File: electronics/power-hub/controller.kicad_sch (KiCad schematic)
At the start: 55 parts, among them J6 USB, SW1 RESET, SW2 BOOT, U2 LMR51635YDDCR, U3 AMS1117-3.3, U4 ESP32-S3-MINI-1-N8, U5 USBLC6-2SC6, U6 TCAN1044AV

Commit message: Power hub v0.5: USB-C PD input (AP33772S), 4 layers, rows off until enabled
The rack now runs from one USB PD 3.1 charger instead of the GST60A24 brick.

Hub v0.5 (76 x 140 mm, 4 layers, In1 GND, In2 VRACK/+3V3):
* AP33772S sink: 20 V at power-up (VSEL 39k), 28 V EPR on the controller's
  request, never 36/48 V; 5 mOhm Kelvin shunt, back-to-back IRF7842 switch,
  SMAJ30A TVS, NTC by the switch, interrupt and I2C to the ESP32-S3.
* USB4105 5 A receptacle; the controller's buck runs from VBUS (5-28 V),
  ahead of the switch.
* Every row's TPS26600 is off until the controller drives ROW_EN (SHDN pulled
  low); IMON per row; front PD LED.
* ERC 0, DRC 0 errors, 0 unconnected, parity 0; 146 3D models, 0 stand-ins.

Power box: 84 x 148 x 35 mm, hub only (no brick, no cradles), rear USB-C
cut-out, lid on corner lugs.  Viewer, BOM (charger + 5 A e-marked cable,
4-layer JLC estimate) and docs (power, mechanical, cabling, assembly,
electronics) follow.

Co-Authored-By: Claude Opus 5.5 <noreply@anthropic.com>
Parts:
- added TP8: PD_VCC, TestPoint:TestPoint_Pad_D1.5mm, symbol Connector:TestPoint
- C118, C119: LCSC (none) -> C53987; MPN (none) -> 0603B472K500NT; Manufacturer (none) -> FH (Guangdong Fenghua Advanced Tech)
- J6: footprint Connector_USB:USB_C_Receptacle_HRO_TYPE-C-31-M-12 -> Connector_USB:USB_C_Receptacle_GCT_USB4105-xx-A_16P_TopMnt_Horizontal; LCSC C165948 -> C5184243; MPN TYPE-C-31-M-12 -> USB4105-GF-A-120; Manufacturer Korean Hroparts -> GCT
- R205: value 1M -> 100k; LCSC C22935 -> C25803; MPN 0603WAF1004T5E -> 0603WAF1003T5E
- R206: value 100k -> 47k; LCSC C25803 -> C25819; MPN 0603WAF1003T5E -> 0603WAF4702T5E
- R211: LCSC (none) -> C23138; MPN (none) -> 0603WAF3300T5E; Manufacturer (none) -> UNI-ROYAL(Uniroyal Elec)
- R215, R216, R217, R218: value 62 -> 56; footprint Resistor_SMD:R_0805_2012Metric -> Resistor_SMD:R_0603_1608Metric; LCSC (none) -> C25196; MPN (none) -> 0603WAF560JT5E; Manufacturer (none) -> UNI-ROYAL(Uniroyal Elec)
- TP6: value +24V -> VRACK
- U3: value AMS1117-3.3 -> AP2112K-3.3TRG1; footprint Package_TO_SOT_SMD:SOT-223-3_TabPin2 -> Package_TO_SOT_SMD:SOT-23-5; symbol Regulator_Linear:AMS1117-3.3 -> Regulator_Linear:AP2112K-3.3; LCSC C6186 -> C51118; MPN AMS1117-3.3 -> AP2112K-3.3TRG1; Manufacturer AMS -> Diodes Incorporated
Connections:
- net ROW_OFF_A is gone; now on net POS_B: U4.15 (IO11)
- net ROW_OFF_B is gone; now on net POS_C: U4.16 (IO12)
- net ROW_OFF_C is gone; now on net POS_D: U4.17 (IO13)
- net +3V3: now also U3.5 (VOUT); no longer U3.2 (VO)
- net +5V: now also U3.1 (VIN)
- net CAN_RXD: now also U4.12 (IO8); no longer U4.36 (IO40)
- net CAN_STB: now also U4.13 (IO9); no longer U4.38 (IO42)
- net CAN_TXD: now also U4.11 (IO7); no longer U4.35 (IO39)
- net CTL_LED: now also U4.31 (IO35); no longer U4.37 (IO41)
- net FLT_A: now also U4.22 (IO18); no longer U4.11 (IO7)
- net FLT_B: now also U4.25 (IO21); no longer U4.12 (IO8)
- net FLT_C: now also U4.27 (IO47); no longer U4.13 (IO9)
- net FLT_D: now also U4.28 (IO33); no longer U4.14 (IO10)
- net GND: now also U3.2 (GND); no longer U3.1 (GND)
- net POS_A: now also U4.14 (IO10); no longer U4.19 (IO15)
- net POS_B: no longer U4.20 (IO16)
- net POS_C: no longer U4.21 (IO17)
- net POS_D: no longer U4.22 (IO18)
- net +24V renamed PD_VCC
- net PD_VCC: now also TP8.1; no longer TP6.1
- net ROW_OFF_D renamed ROW_EN_A
- net VBUS renamed USB_VBUS
- net VSENSE renamed VBUS_SENSE
- new net I2C_PU: U4.38 (IO42)
- new net PD_INT: U4.35 (IO39)
- new net PD_SCL: U4.36 (IO40)
- new net PD_SDA: U4.37 (IO41)
- new net ROW_EN_B: U4.19 (IO15)
- new net ROW_EN_C: U4.20 (IO16)
- new net ROW_EN_D: U4.21 (IO17)
- new net VRACK: TP6.1
- no-connect marks 15 -> 11
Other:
- note added: "5 V buck: LMR51635, as the bay node (TI SLUSF64B table 8-2), from VBUS ahead of the switch"
- note added: "5 V for the controller: the buck or the console USB-C (diode OR), 3.3 V low-dropout LDO"
- note added: "USB-C: the controller's console / firmware (native USB), and its 5 V without a PD charger"
- note removed: "5 V buck: LMR51635, as the bay node (TI SLUSF64B table 8-2)"
- note removed: "5 V for the controller: the buck or the USB-C (diode OR), 3.3 V LDO"
- note removed: "USB-C: the controller's console / firmware (native USB), and its 5 V when 24 V is off"
- moved on the sheet: C104, C105, C106, C107, C108, C109, C110, C111, C112, C113, C114, C116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

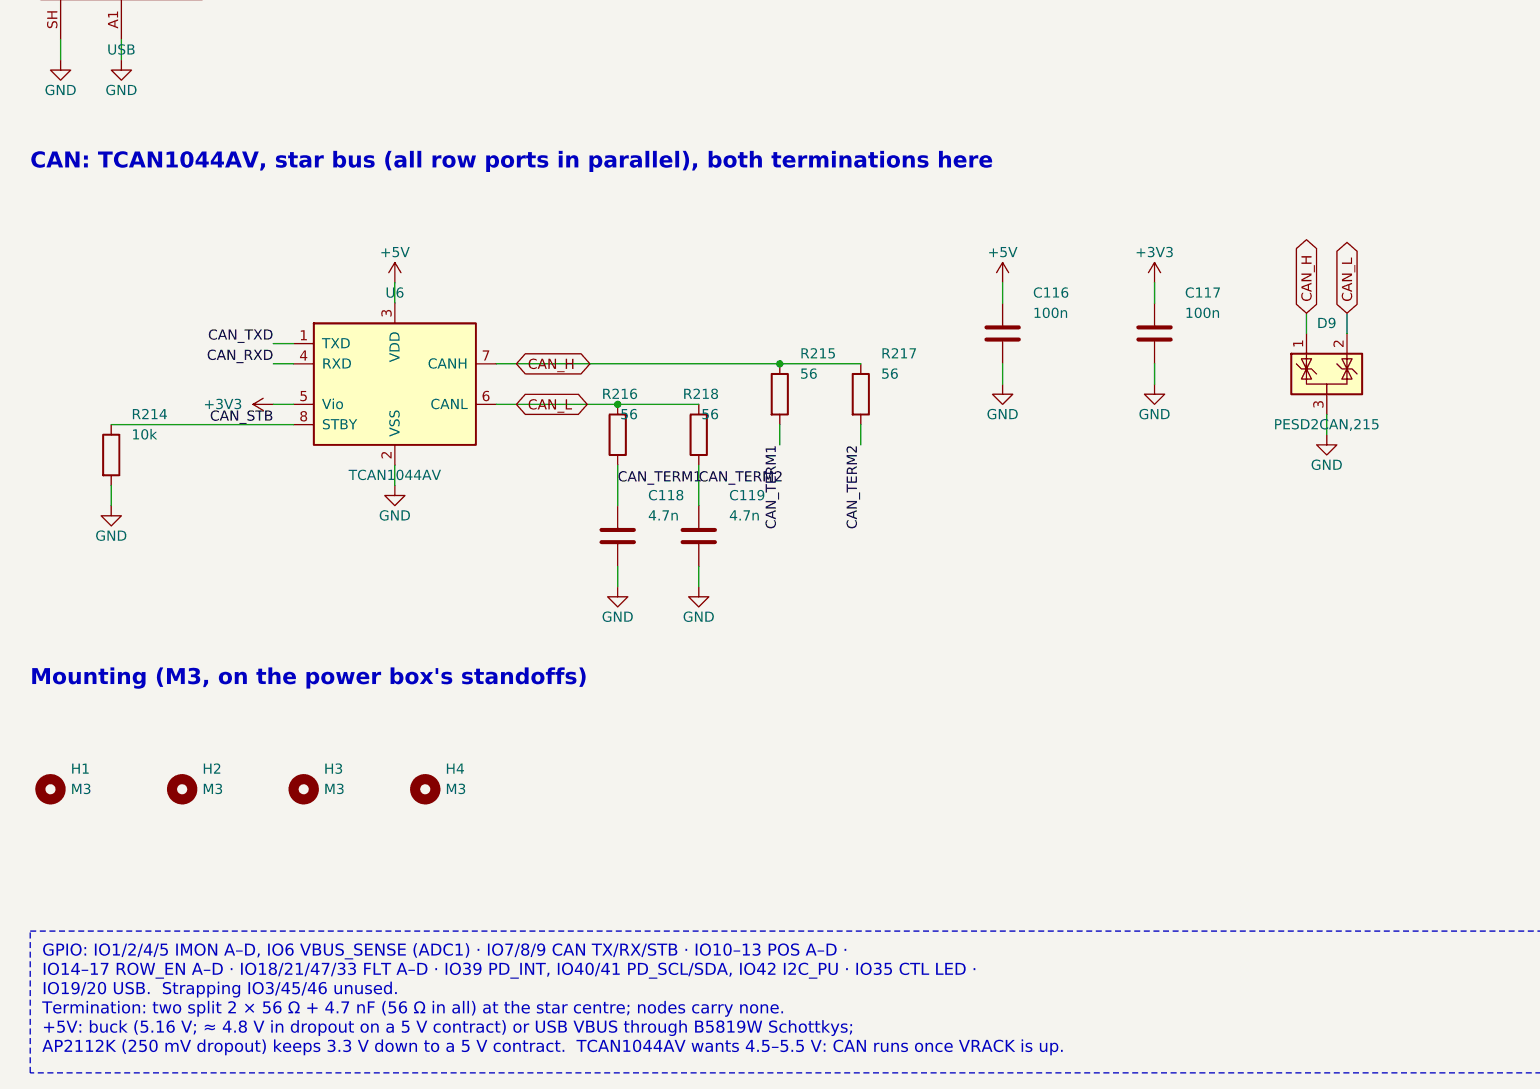
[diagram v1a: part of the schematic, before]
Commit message: CAN transceiver: TCAN1462V (signal improvement) on the hub and the bay node
Same SOIC-8 pinout as the TCAN1044AV (VIO on pin 5, STB on pin 8), so the
footprint, placement and routing are unchanged: the regenerated PCBs keep
every track and via, only U6 / U11's value and fields change.  Signal
improvement (CiA 601-4, ISO 11898-2:2024 set C) damps the ringing of the
star's open branch ends; the termination (56 ohm at the hub) stays.

* catalog: TCAN1462VDRQ1 (C7399456, no LCSC stock on 2026-10-18), with the
  TCAN1044AVDRQ1 (C3234993) and NXP TJA1462AT/0Z (C3234095) as alternates;
  CPL rotation for all three.
* BOM: the board BOMs' alternates now show in the rack BOM notes; JLC
  estimates +$0.54 per board.
* docs/can.md: why the star is fine at 250 kbit/s and what SIC adds, with
  sources (TI SLLSFF2B, SLLA581A; CiA bit-timing table; NXP TJA1462).
* Both boards: ERC 0, DRC 0 errors, 0 unconnected, parity 0; 3D 0 stand-ins.

Co-Authored-By: Claude Opus 5.5 <noreply@anthropic.com>
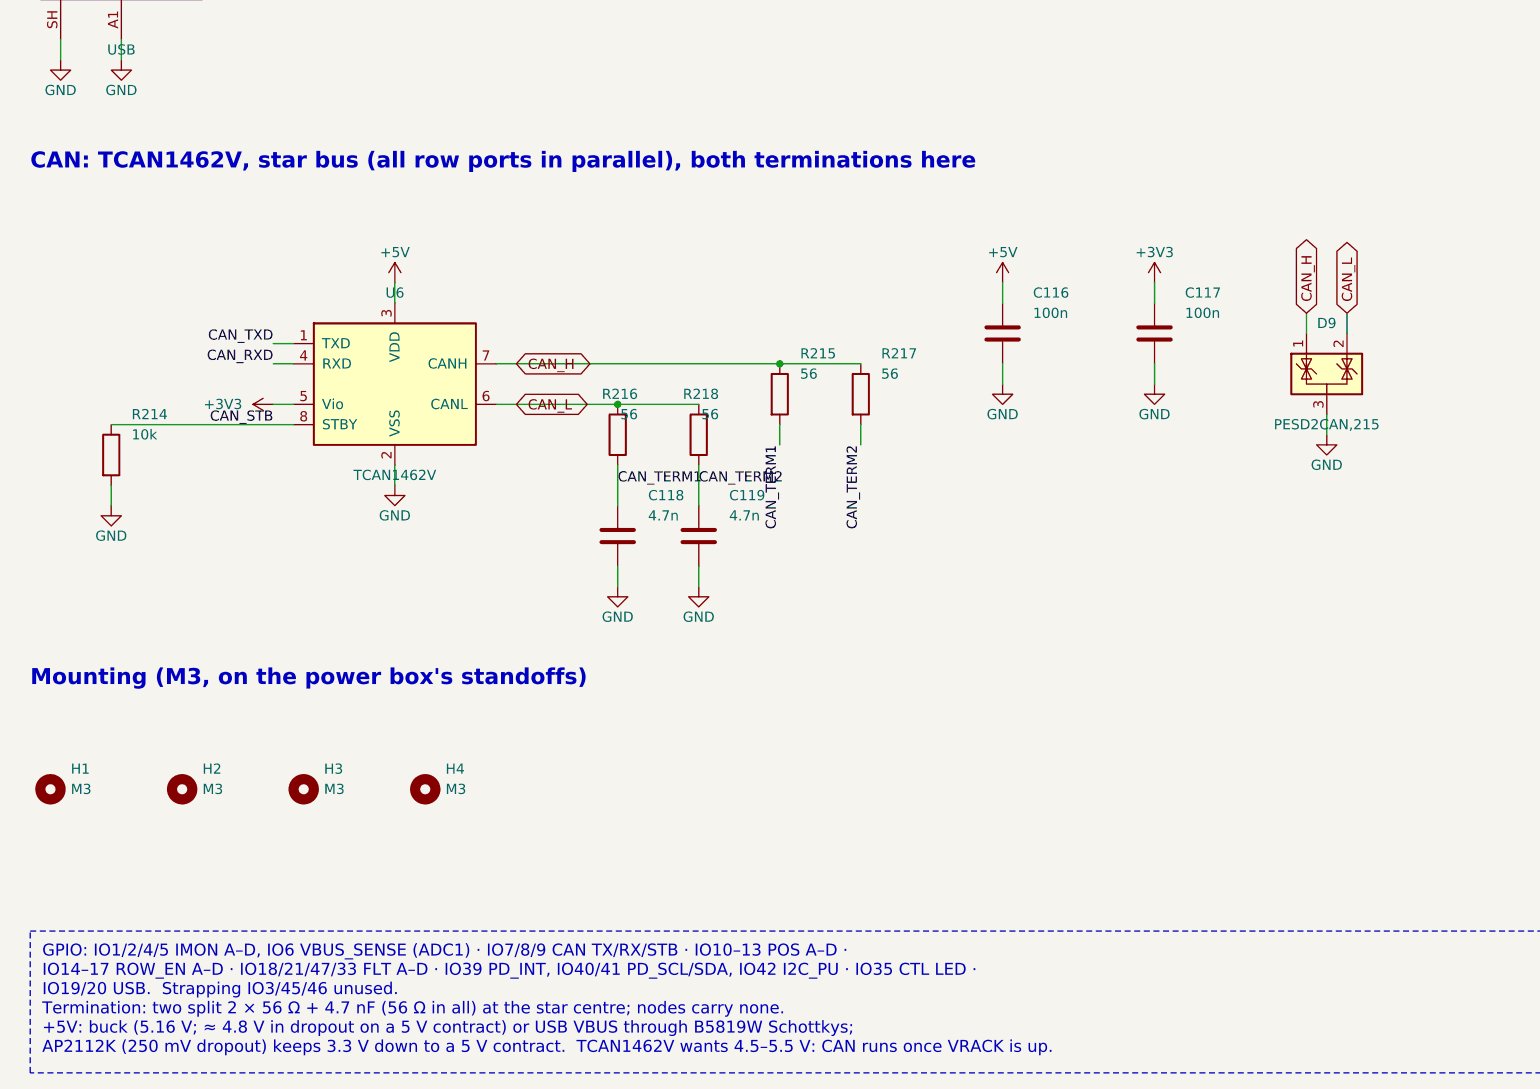
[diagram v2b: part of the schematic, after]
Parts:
- U6: value TCAN1044AV -> TCAN1462V; Alternative (none) -> LCSC stock was 0 on 2026-10-18. Same pinout: TCAN1044AVDRQ1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; LCSC C3234993 -> C7399456; MPN TCAN1044AVDRQ1 -> TCAN1462VDRQ1
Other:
- note added: "CAN: TCAN1462V, star bus (all row ports in parallel), both terminations here"
- note removed: "CAN: TCAN1044AV, star bus (all row ports in parallel), both terminations here"
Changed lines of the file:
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@@
 		)
 	)
-	(text "CAN: TCAN1044AV, star bus (all row ports in parallel), both terminations here"
+	(text "CAN: TCAN1462V, star bus (all row ports in parallel), both terminations here"
 		(exclude_from_sim no)
 		(at 20.32 320.04 0)
@@
 			)
 		)
-		(property "Value" "TCAN1044AV"
+		(property "Value" "TCAN1462V"
 			(at 66.04 358.14 0)
 			(effects
@@
 			)
 		)
-		(property "Datasheet" "https://www.ti.com/lit/ds/symlink/tcan1044av-q1.pdf"
+		(property "Datasheet" "https://www.ti.com/lit/ds/symlink/tcan1462-q1.pdf"
 			(at 66.04 346.71 0)
 			(effects
@@
 			)
 		)
-		(property "Description" "CAN FD transceiver, VCC 5 V, VIO 1.8–5 V, bus pins ±58 V (MCP2562 pinout)"
+		(property "Description" "CAN FD SIC transceiver, VCC 5 V, VIO 1.7–5.5 V, bus pins ±58 V (MCP2562 pinout)"
 			(at 66.04 346.71 0)
 			(effects
@@
 			)
 		)
-		(property "MPN" "TCAN1044AVDRQ1"
+		(property "MPN" "TCAN1462VDRQ1"
 			(at 66.04 346.71 0)
 			(effects
@@
 			)
 		)
-		(property "LCSC" "C3234993"
+		(property "LCSC" "C7399456"
+			(at 66.04 346.71 0)
+			(effects
+				(font
+					(size 1.27 1.27)
+				)
+				(hide yes)
+			)
+		)
+		(property "Alternative" "LCSC stock was 0 on 2026-10-18.  Same pinout: TCAN1044AVDRQ1 (C3234993, no SIC, ±58 V) or NXP TJA1462AT/0Z (C3234095, SIC, VIO 2.95–5.5 V, bus pins −36/+40 V)"
 			(at 66.04 346.71 0)
 			(effects
@@
 		)
 	)
-	(text_box "GPIO: IO1/2/4/5 IMON A–D, IO6 VBUS_SENSE (ADC1) · IO7/8/9 CAN TX/RX/STB · IO10–13 POS A–D ·\n  IO14–17 ROW_EN A–D · IO18/21/47/33 FLT A–D · IO39 PD_INT, IO40/41 PD_SCL/SDA, IO42 I2C_PU · IO35 CTL LED ·\n  IO19/20 USB.  Strapping IO3/45/46 unused.\nTermination: two split 2 × 56 Ω + 4.7 nF (56 Ω in all) at the star centre; nodes carry none.\n+5V: buck (5.16 V; ≈ 4.8 V in dropout on a 5 V contract) or USB VBUS through B5819W Schottkys;\n  AP2112K (250 mV dropout) keeps 3.3 V down to a 5 V contract.  TCAN1044AV wants 4.5–5.5 V: CAN runs once VRACK is up."
+	(text_box "GPIO: IO1/2/4/5 IMON A–D, IO6 VBUS_SENSE (ADC1) · IO7/8/9 CAN TX/RX/STB · IO10–13 POS A–D ·\n  IO14–17 ROW_EN A–D · IO18/21/47/33 FLT A–D · IO39 PD_INT, IO40/41 PD_SCL/SDA, IO42 I2C_PU · IO35 CTL LED ·\n  IO19/20 USB.  Strapping IO3/45/46 unused.\nTermination: two split 2 × 56 Ω + 4.7 nF (56 Ω in all) at the star centre; nodes carry none.\n+5V: buck (5.16 V; ≈ 4.8 V in dropout on a 5 V contract) or USB VBUS through B5819W Schottkys;\n  AP2112K (250 mV dropout) keeps 3.3 V down to a 5 V contract.  TCAN1462V wants 4.5–5.5 V: CAN runs once VRACK is up."
 		(exclude_from_sim no)
 		(at 20.32 415.29 0)
